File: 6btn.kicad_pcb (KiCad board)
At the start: 2 copper layers, 50 x 26.3 mm, 46 parts, among them CON1 AVR-ISP, IC1 ATTINY88-A, Q1 2N7002, Q2 2N7002, U1 74HC14D_653, U2 SW_SPST, U3 SW_SPST, U4 SW_SPST, U5 SW_SPST, U6 SW_SPST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

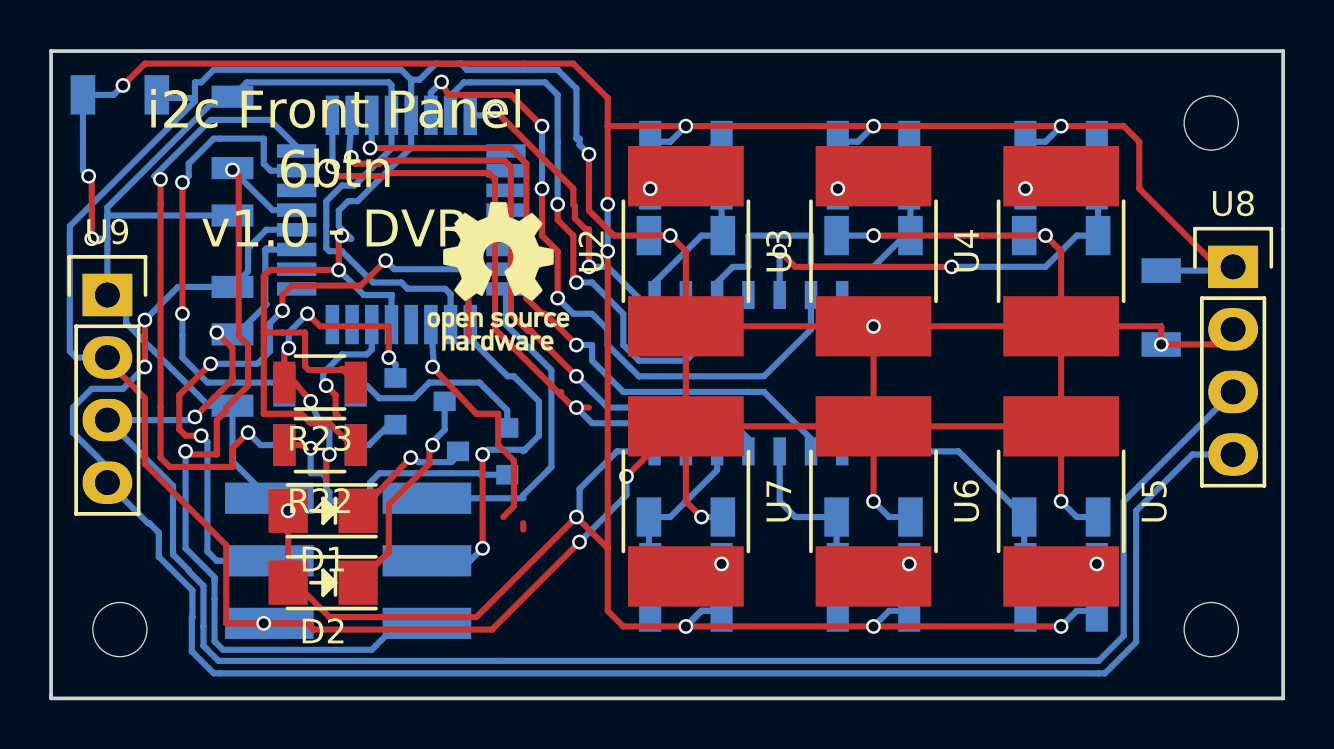
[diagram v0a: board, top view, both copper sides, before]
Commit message: Headers aligned better
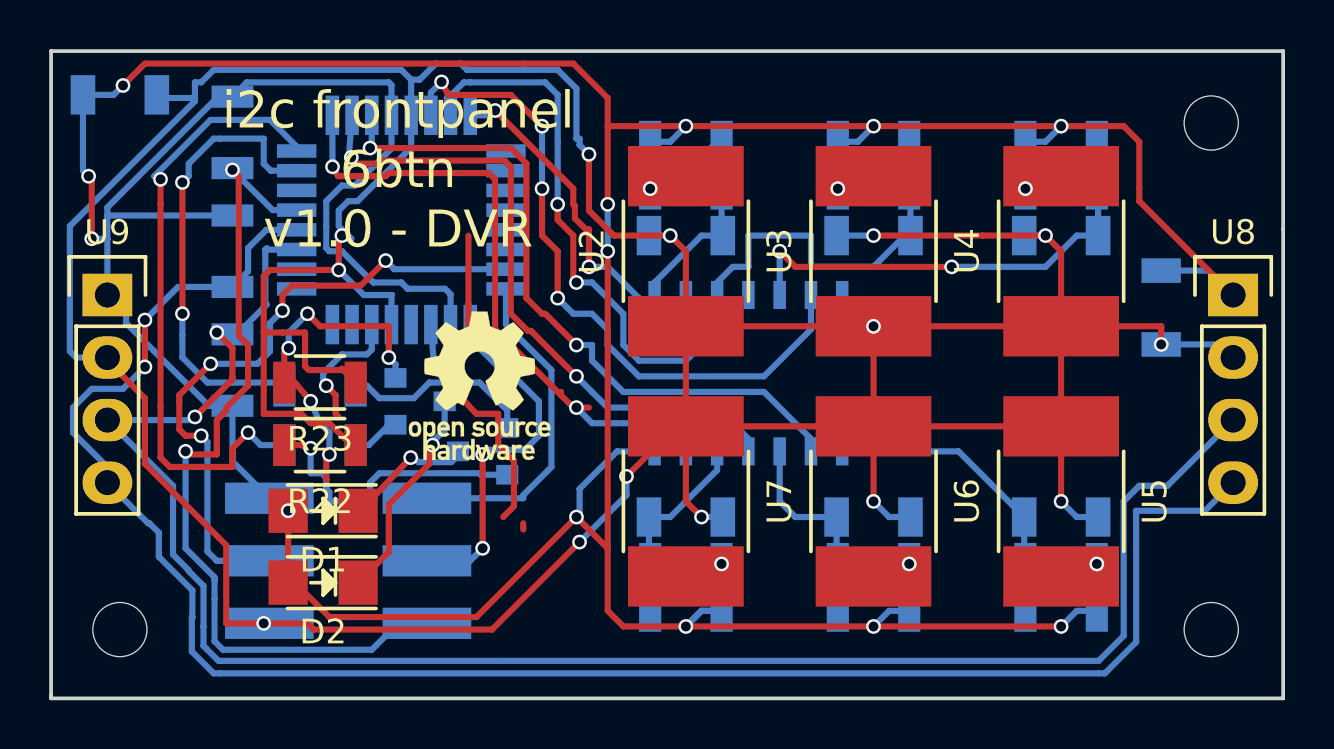
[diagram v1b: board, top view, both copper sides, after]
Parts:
- moved REF*** 4.51 mm to (50.2, 34.7)
- moved U8 1.14 mm to (80.8, 31.0)
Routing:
- net VCC: track 186.8 -> 187.9 mm
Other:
- board text added: "i2c frontpanel 6btn v1.0 - DVR"
- board text removed: "i2c Front Panel 6btn v1.0 - DVR"
